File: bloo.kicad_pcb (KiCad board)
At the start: 2 copper layers, 90 x 96 mm, 95 parts, among them J5 SWD_Header, M1 M1_Conn_Alt, M2 M2_Conn_Alt, Q0 TEFT4300, Q1 TEFT4300, Q10 Q_NMOS_GSD, Q11 Q_NMOS_GSD, Q12 Q_NMOS_GSD, Q2 TEFT4300, Q3 TEFT4300, Q9 Q_NMOS_GSD, SW1 SW, SW2 SW, U1 YAAJ_BluePill_SWD_Breakout, U2 L293D, U3 LM1085-5.0, U4 NCP161ASN330T1G, U5 BC832, Y1 ABS07-32.768KHZ-T

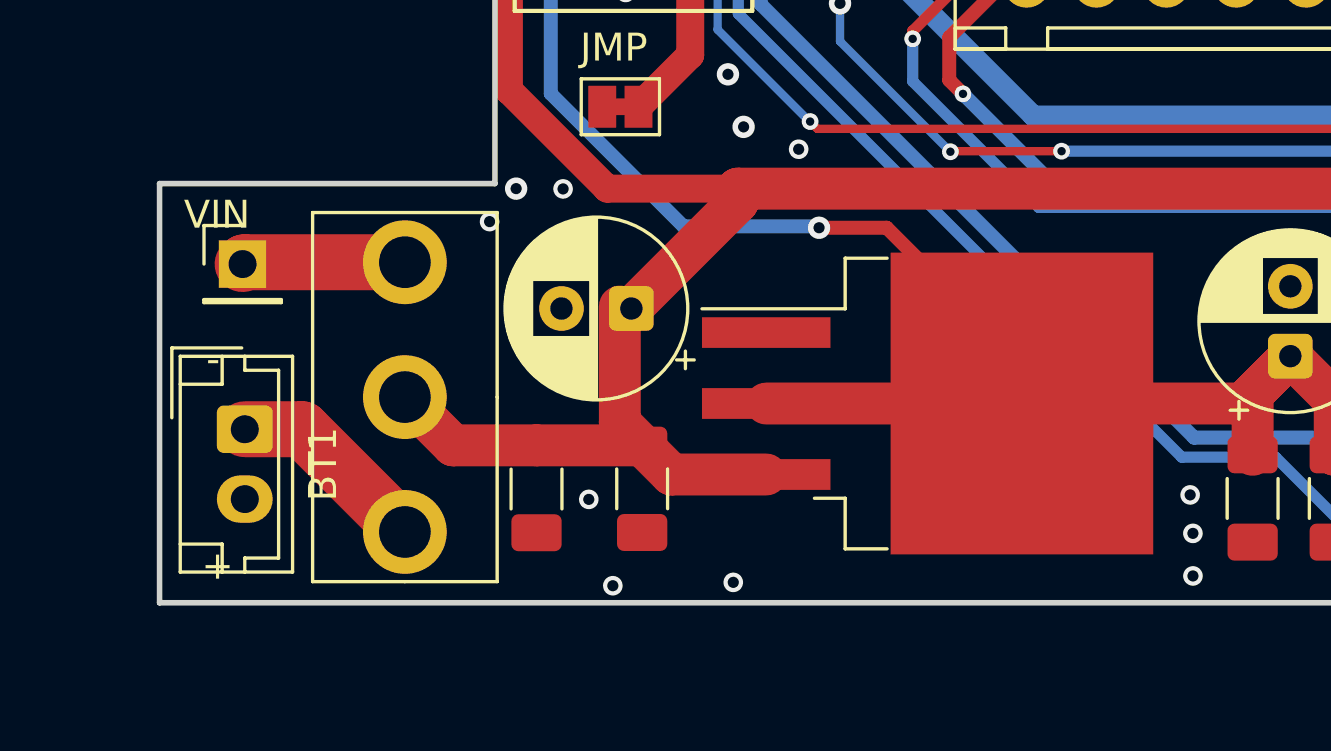
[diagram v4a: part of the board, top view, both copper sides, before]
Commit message: updated correct jst battery connector
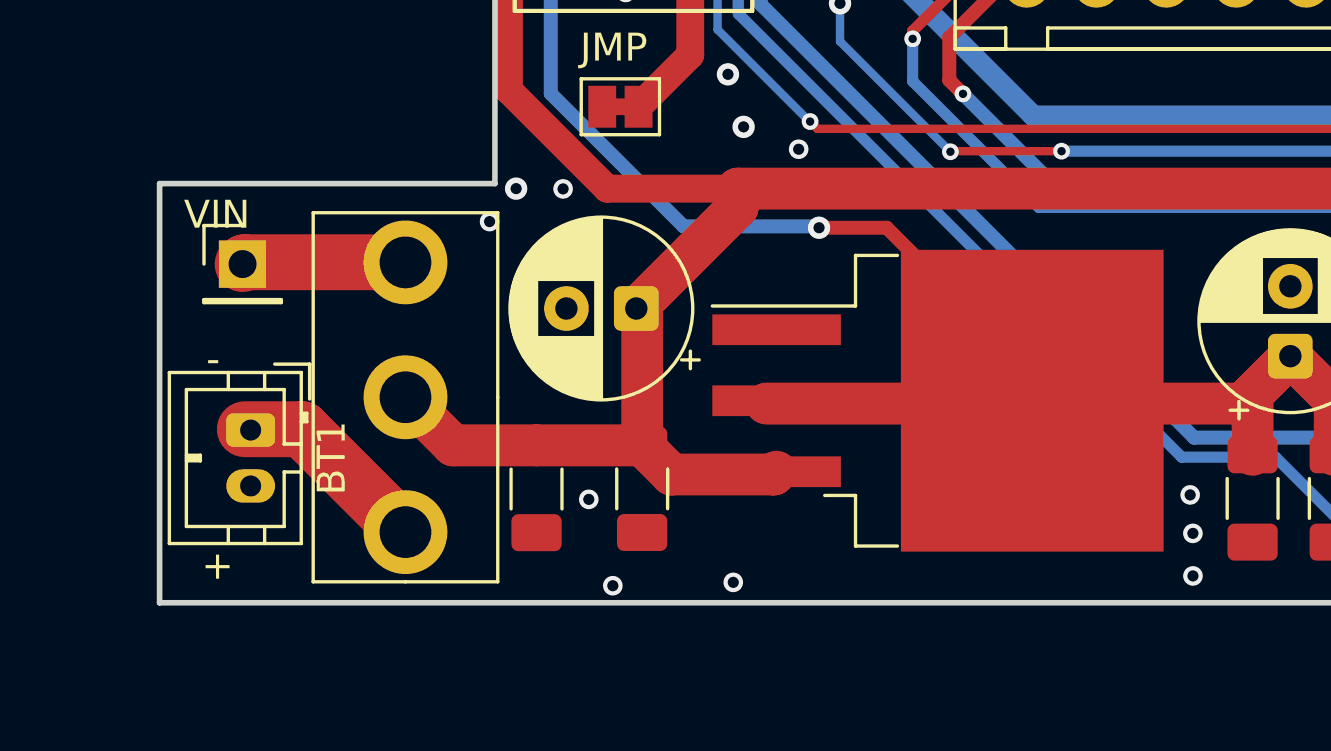
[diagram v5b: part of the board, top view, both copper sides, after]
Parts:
- BT1: footprint Connector_JST:JST_EH_B2B-EH-A_1x02_P2.50mm_Vertical -> Connector_JST:JST_PH_B2B-PH-K_1x02_P2.00mm_Vertical
- moved U3 0.38 mm to (237.4, 135.9)
- moved BT1 0.21 mm to (212.8, 128.9)
- moved C2 0.18 mm to (226.6, 124.6)

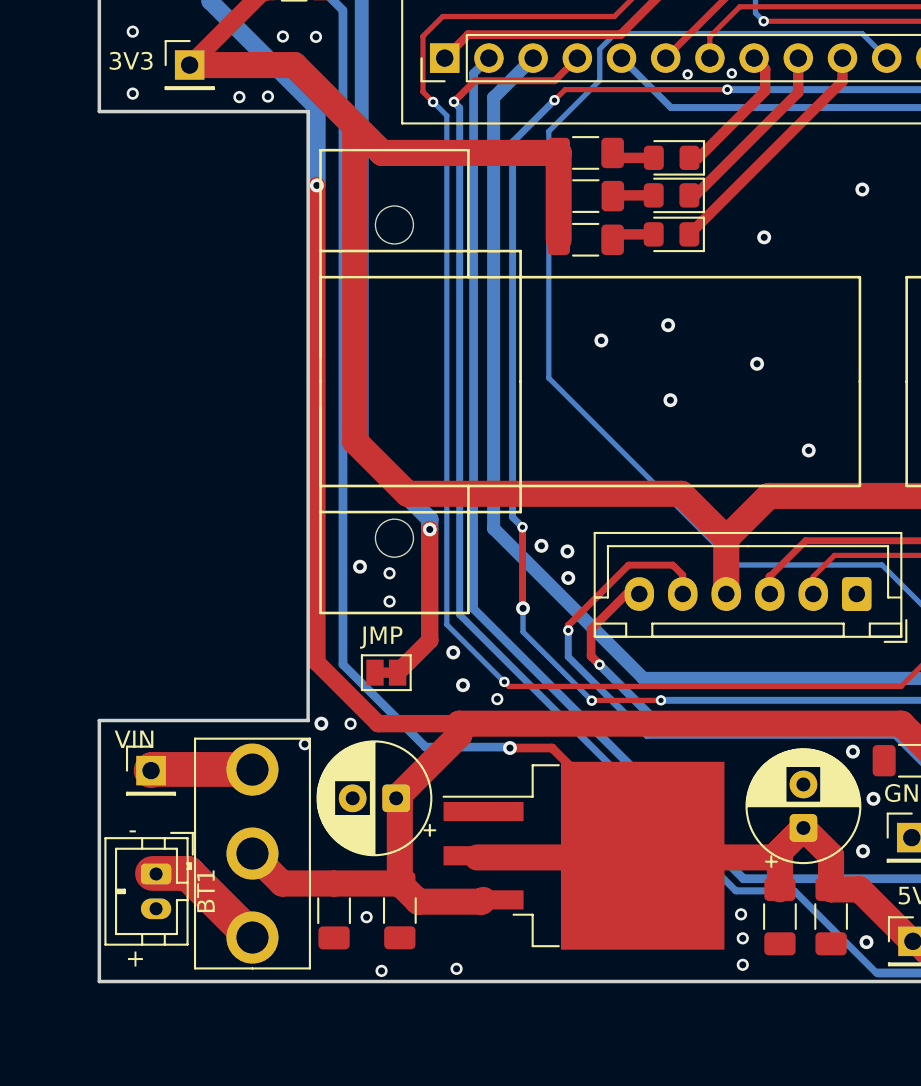
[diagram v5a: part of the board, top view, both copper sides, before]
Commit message: switched to xt30 battery footprint
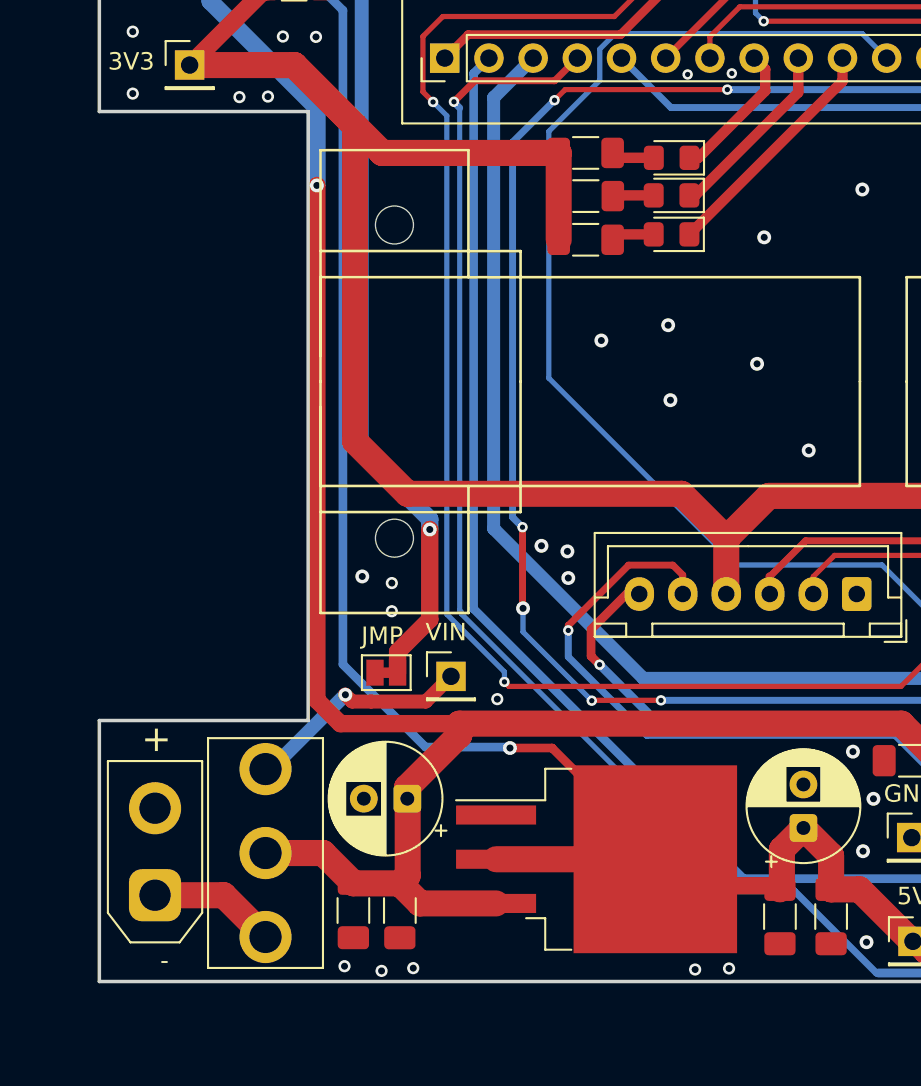
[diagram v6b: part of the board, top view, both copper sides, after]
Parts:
- BT1: footprint Connector_JST:JST_PH_B2B-PH-K_1x02_P2.00mm_Vertical -> Connector_AMASS:AMASS_XT30UPB-M_1x02_P5.0mm_Vertical
- moved TP1 18.1 mm to (229.7, 117.6)
- moved BT1 1.22 mm to (212.7, 130.1), turned to 90 degrees
- moved C9 1.11 mm to (224.1, 131.0)
- moved S1 0.75 mm to (213.9, 127.7)
- moved U3 0.75 mm to (238.1, 136.1)
- moved C2 0.64 mm to (227.2, 124.6)
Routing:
- net Net-(S1-Pad3): track 5.84 -> 13.2 mm, vias 0 -> 1
- net +5V: track 244.7 -> 242.3 mm
- net VCC: track 171.5 -> 172.5 mm
- net GND: vias 118 -> 112
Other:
- board text removed: "+"
